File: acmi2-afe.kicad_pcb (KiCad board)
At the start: 10 copper layers, 241.3 x 101.6 mm, 117 parts, among them J1 6469028-1, J2 6469028-1, J3 6469028-1, J4 Conn_Coaxial, J5 5499922-4, J6 39301022, J7 5499922-4, Q1 NX7002BKW, T1 T1-1T-KK81, U1 200MHz, U2 LTC2107CUK-PBF, U3 TPS7A8500RGRT, U4 TPSM82866AA0HRDMR, U5 TPS7A8500RGRT, U6 TPS259540DSGR, U7 SN74LVC16T245DGGR, U8 CAT25320VI-GT3

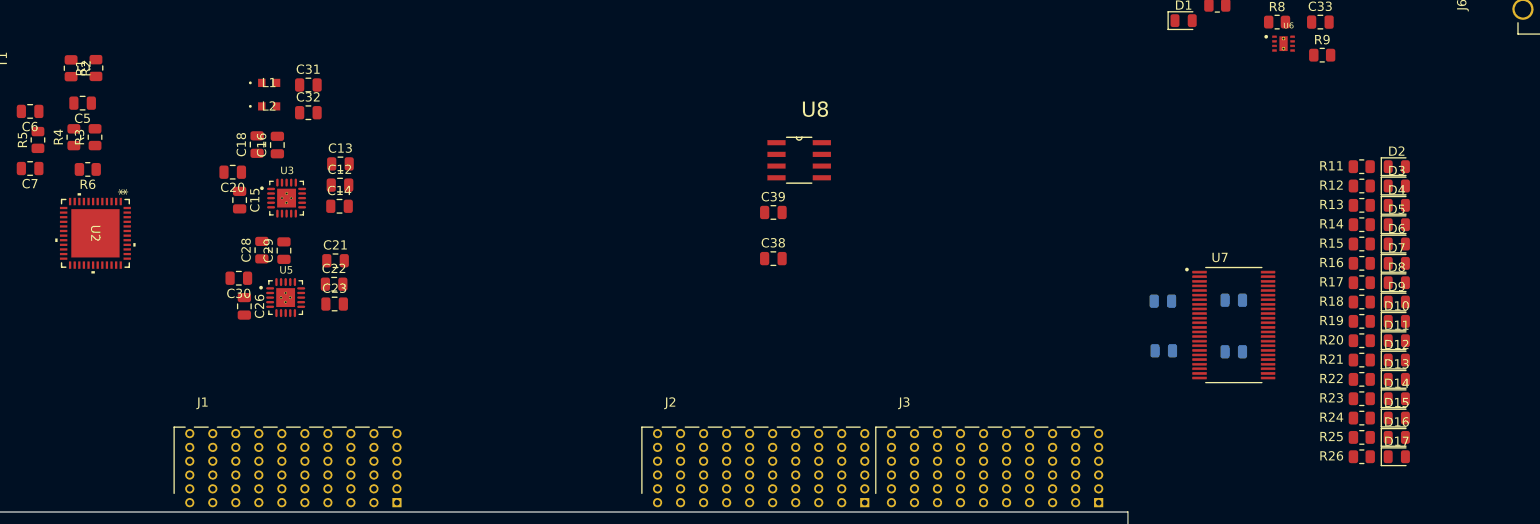
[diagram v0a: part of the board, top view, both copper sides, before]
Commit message: Untangled adc data connections
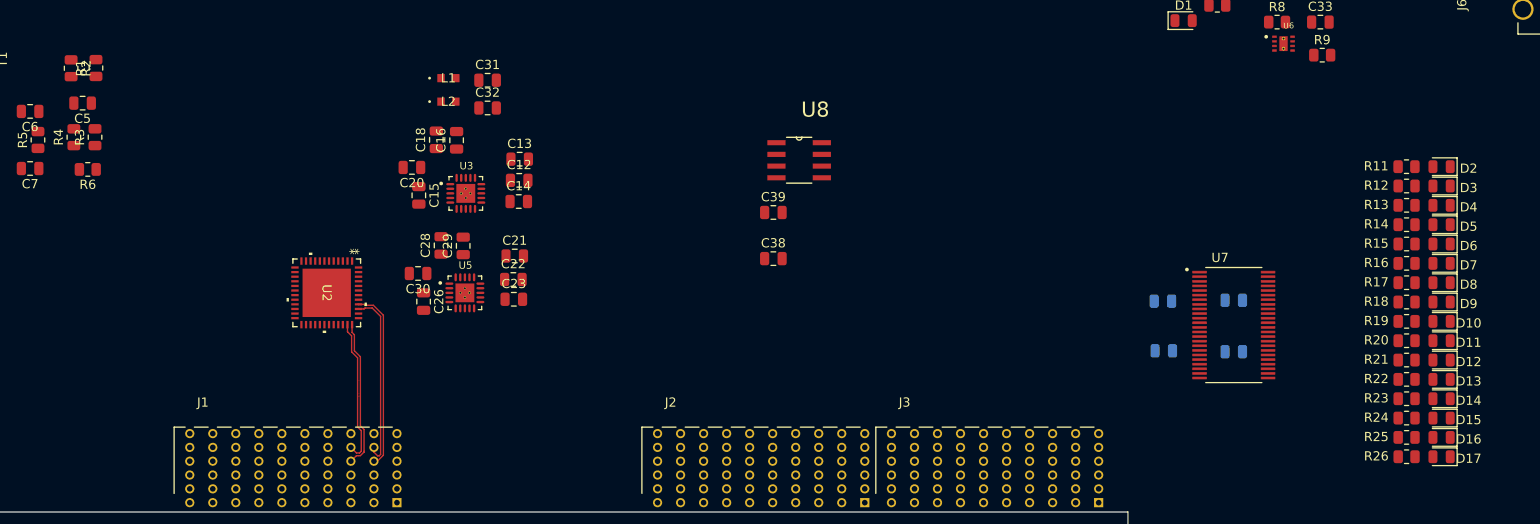
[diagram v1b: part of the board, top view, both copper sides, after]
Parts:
- moved U2 25.9 mm to (159.2, 298.5)
- moved C12 19.5 mm to (180.1, 286.3)
- moved C13 19.5 mm to (180.2, 284.0)
- moved C14 19.5 mm to (180.1, 288.6)
- moved C16 19.5 mm to (173.3, 281.9)
- moved C18 19.5 mm to (171.1, 281.9)
- moved C21 19.5 mm to (179.6, 294.5)
- moved C22 19.5 mm to (179.5, 297.1)
- moved C26 19.5 mm to (169.7, 299.4)
- moved C28 19.5 mm to (171.6, 293.4)
- moved C30 19.5 mm to (169.1, 296.4)
- moved C31 19.5 mm to (176.7, 275.4)
- moved C32 19.5 mm to (176.7, 278.4)
- moved L1 19.5 mm to (172.4, 275.2)
- moved L2 19.5 mm to (172.4, 277.7)
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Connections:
- J1 pad A1: /adc/D0_P -> /adc/CSN
- J1 pad A2: /adc/D4_P -> /adc/SDI
- J1 pad A3: /adc/D8_P -> /adc/D14_P
- J1 pad A4: /adc/D12_P -> /adc/D10_P
- J1 pad A6: /adc/SDO -> /adc/D6_P
- J1 pad A7: unconnected-(J1-PadA7) -> /adc/D2_P
- J1 pad A8: unconnected-(J1-PadA8) -> /adc/SDO
- J1 pad B1: /adc/D0_N -> unconnected-(J1-PadB1)
- J1 pad B2: /adc/D4_N -> unconnected-(J1-PadB2)
- J1 pad B3: /adc/D8_N -> /adc/D14_N
- J1 pad B4: /adc/D12_N -> /adc/D10_N
- J1 pad B6: /adc/SDI -> /adc/D6_N
- J1 pad B7: unconnected-(J1-PadB7) -> /adc/D2_N
- J1 pad C1: /adc/D2_P -> /adc/SCK
- J1 pad C2: /adc/D6_P -> /adc/OF_P
- J1 pad C3: /adc/D10_P -> /adc/D12_P
- J1 pad C4: /adc/D14_P -> unconnected-(J1-PadC4)
- J1 pad C5: /adc/OF_P -> /adc/D8_P
- J1 pad C6: /adc/SCK -> /adc/D4_P
- J1 pad C7: unconnected-(J1-PadC7) -> /adc/D0_P
- J1 pad D1: /adc/D2_N -> unconnected-(J1-PadD1)
- J1 pad D2: /adc/D6_N -> /adc/OF_N
- J1 pad D3: /adc/D10_N -> /adc/D12_N
- J1 pad D4: /adc/D14_N -> unconnected-(J1-PadD4)
- J1 pad D5: /adc/OF_N -> /adc/D8_N
- J1 pad D6: /adc/CSN -> /adc/D4_N
- J1 pad D7: unconnected-(J1-PadD7) -> /adc/D0_N
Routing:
- net /adc/OF_P: track 0.00 -> 19.7 mm
- net /adc/OF_N: track 0.00 -> 19.3 mm
- net /adc/D12_P: track 0.00 -> 16.3 mm
- net /adc/D12_N: track 0.00 -> 15.8 mm

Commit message: push from windows
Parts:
- moved J7 1.40 mm to (111.2, 241.9)
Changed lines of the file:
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@@
 	(footprint "My Footprints:TE_5499922-4"
 		(layer "F.Cu")
-		(at 112.480468 242.555)
+		(at 111.24 241.9)
 		(property "Reference" "J7"
 			(at -8.745 -7.435 0)

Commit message: Finish routing
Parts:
- removed TP5, TP6: GND, My Footprints:TestPoint_RCS-0C
- added C40: 0.1u, Capacitor_SMD:C_0805_2012Metric, F.Cu at (119.4, 294.0)
- C1, C11, C39: moved to B.Cu
- moved G*** 187.4 mm to (87.2, 277.4)
- moved TP2 85.0 mm to (259.4, 332.0)
- moved C17 74.8 mm to (278.6, 320.9), turned to -90 degrees
- moved C19 74.7 mm to (276.4, 320.9), turned to -90 degrees
- moved C38 71.4 mm to (274.2, 320.9), turned to -90 degrees
- moved C24 67.1 mm to (265.9, 322.1), turned to 90 degrees
- moved U4 65.9 mm to (269.9, 320.7), turned to -90 degrees
- moved C25 63.8 mm to (263.6, 322.1), turned to 90 degrees
- moved R7 63.3 mm to (269.6, 316.0)
- moved C27 60.5 mm to (261.3, 322.1), turned to 90 degrees
- moved R9 60.2 mm to (285.4, 330.1), turned to -90 degrees
- moved R8 58.9 mm to (281.4, 324.8), turned to -90 degrees
- moved C33 58.6 mm to (285.4, 324.8), turned to -90 degrees
- moved Q1 57.7 mm to (276.7, 315.2)
- moved C10 57.1 mm to (166.2, 298.1), turned to 90 degrees
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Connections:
- net Net-(J6-Pad2) renamed /Regulators/+5VIN
- net Net-(U3-EN) renamed /Regulators/+3.3v_U3
- net Net-(U5-EN) renamed /Regulators/+3.3v_U5
- C3 pad 2: /adc/adc_clk_p -> /adc/ADC_CLK_P
- C4 pad 2: /adc/adc_clk_n -> /adc/ADC_CLK_N
- J2 pad A1: /Fault LED's/fault_led0 -> unconnected-(J2-PadA1)
- J2 pad A2: /Fault LED's/fault_led4 -> unconnected-(J2-PadA2)
- J2 pad A3: /Fault LED's/fault_led8 -> unconnected-(J2-PadA3)
- J2 pad A4: /Fault LED's/fault_led12 -> unconnected-(J2-PadA4)
- J2 pad B1: /Fault LED's/fault_led1 -> unconnected-(J2-PadB1)
- J2 pad B2: /Fault LED's/fault_led5 -> unconnected-(J2-PadB2)
- J2 pad B3: /Fault LED's/fault_led9 -> unconnected-(J2-PadB3)
- J2 pad B4: /Fault LED's/fault_led13 -> unconnected-(J2-PadB4)
- J2 pad C1: /Fault LED's/fault_led2 -> unconnected-(J2-PadC1)
- J2 pad C10: unconnected-(J2-PadC10) -> /Fault LED's/fault_led1
- J2 pad C2: /Fault LED's/fault_led6 -> unconnected-(J2-PadC2)
- J2 pad C3: /Fault LED's/fault_led10 -> /Fault LED's/fault_led15
- J2 pad C4: /Fault LED's/fault_led14 -> /Fault LED's/fault_led13
- J2 pad C5: unconnected-(J2-PadC5) -> /Fault LED's/fault_led11
- J2 pad C6: unconnected-(J2-PadC6) -> /Fault LED's/fault_led9
- J2 pad C7: unconnected-(J2-PadC7) -> /Fault LED's/fault_led7
- J2 pad C8: unconnected-(J2-PadC8) -> /Fault LED's/fault_led5
- J2 pad C9: unconnected-(J2-PadC9) -> /Fault LED's/fault_led3
- J2 pad D1: /Fault LED's/fault_led3 -> unconnected-(J2-PadD1)
- J2 pad D10: unconnected-(J2-PadD10) -> /Fault LED's/fault_led0
- J2 pad D2: /Fault LED's/fault_led7 -> unconnected-(J2-PadD2)
- J2 pad D3: /Fault LED's/fault_led11 -> /Fault LED's/fault_led14
- J2 pad D4: /Fault LED's/fault_led15 -> /Fault LED's/fault_led12
- J2 pad D5: unconnected-(J2-PadD5) -> /Fault LED's/fault_led10
- J2 pad D6: unconnected-(J2-PadD6) -> /Fault LED's/fault_led8
- J2 pad D7: unconnected-(J2-PadD7) -> /Fault LED's/fault_led6
- J2 pad D8: unconnected-(J2-PadD8) -> /Fault LED's/fault_led4
- J2 pad D9: unconnected-(J2-PadD9) -> /Fault LED's/fault_led2
- J3 pad A1: /Pulser Interface/tp_pos0 -> /Pulser Interface/tp_neg4
- J3 pad A10: /Relay Board Interface/spare4 -> /Relay Board Interface/faultn
- J3 pad A2: /Pulser Interface/tp_pos4 -> /Pulser Interface/tp_neg0
- J3 pad A3: /Pulser Interface/tp_neg3 -> /Pulser Interface/tp_pos1
- J3 pad A8: /Relay Board Interface/fault_rdbk -> /Relay Board Interface/spare3
- J3 pad A9: /Relay Board Interface/spare0 -> /Relay Board Interface/keylock
- J3 pad B1: /Pulser Interface/tp_pos1 -> /Pulser Interface/tp_neg3
- J3 pad B2: /Pulser Interface/tp_neg0 -> /Pulser Interface/tp_pos4
- J3 pad B3: /Pulser Interface/tp_neg4 -> /Pulser Interface/tp_pos0
- J3 pad B8: /zuDFE Connectors/fault_reset -> /Relay Board Interface/spare2
- J3 pad B9: /Relay Board Interface/spare1 -> /Relay Board Interface/force_trip
- J3 pad C1: /Pulser Interface/tp_pos2 -> /Pulser Interface/tp_neg2
- J3 pad C2: /Pulser Interface/tp_neg1 -> /Pulser Interface/tp_pos3
- J3 pad C8: /Relay Board Interface/force_trip -> /Relay Board Interface/spare1
- J3 pad C9: /Relay Board Interface/spare2 -> /Relay Board Interface/fault_reset
- J3 pad D1: /Pulser Interface/tp_pos3 -> /Pulser Interface/tp_neg1
- J3 pad D2: /Pulser Interface/tp_neg2 -> /Pulser Interface/tp_pos2
- J3 pad D7: /Relay Board Interface/faultn -> /Relay Board Interface/spare4
- J3 pad D8: /Relay Board Interface/keylock -> /Relay Board Interface/spare0
- J3 pad D9: /Relay Board Interface/spare3 -> /Relay Board Interface/fault_rdbk
- R3 pad 1: Net-(U2-AIN+) -> /adc/AIN_N
- R4 pad 1: Net-(U2-AIN-) -> /adc/AIN_P
- R6 pad 1: Net-(U2-AIN+) -> /adc/AIN_N
- R6 pad 2: Net-(U2-AIN-) -> /adc/AIN_P
- T1 pad 4: Net-(C2-Pad2) -> Net-(C40-Pad2)
- T1 pad 6: GND -> Net-(C2-Pad2)
- U2 pad 14: /adc/adc_clk_p -> /adc/ADC_CLK_N
- U2 pad 15: /adc/adc_clk_n -> /adc/ADC_CLK_P
- U2 pad 8: Net-(U2-AIN+) -> /adc/AIN_P
- U2 pad 9: Net-(U2-AIN-) -> /adc/AIN_N
- U3 pad V1: (no net) -> GND
- U3 pad V2: (no net) -> GND
- U3 pad V3: (no net) -> GND
- U3 pad V4: (no net) -> GND
- U4 pad 24: (no net) -> GND
- U4 pad 25: (no net) -> GND
- U4 pad 26: (no net) -> GND
- U4 pad 27: (no net) -> GND
- U5 pad V1: (no net) -> GND
- U5 pad V2: (no net) -> GND
- U5 pad V3: (no net) -> GND
- U5 pad V4: (no net) -> GND
- U6 pad 10: (no net) -> GND
- U6 pad 11: (no net) -> GND
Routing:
- net GND: track 17.4 -> 195.0 mm, vias 6 -> 92
- net /Relay Board Interface/faultn: track 0.00 -> 145.6 mm
- net /Relay Board Interface/keylock: track 0.00 -> 141.5 mm
- net /Relay Board Interface/force_trip: track 0.00 -> 140.9 mm
- net /Relay Board Interface/fault_reset: track 0.00 -> 139.2 mm
- net /Relay Board Interface/fault_rdbk: track 0.00 -> 138.4 mm
- net /Relay Board Interface/spare2: track 0.00 -> 135.0 mm
- net /Relay Board Interface/spare0: track 0.00 -> 133.9 mm
- net /Relay Board Interface/spare3: track 0.00 -> 133.5 mm
- net /Relay Board Interface/spare1: track 0.00 -> 133.5 mm
- net /Relay Board Interface/spare4: track 0.00 -> 126.9 mm
- net /Regulators/afe_pwrenb: track 0.00 -> 117.9 mm, vias 0 -> 1
- net /Fault LED's/fault_led0: track 0.00 -> 85.2 mm, vias 0 -> 1
- net /Fault LED's/fault_led1: track 0.00 -> 84.3 mm, vias 0 -> 1
- net /Fault LED's/fault_led2: track 0.00 -> 81.3 mm, vias 0 -> 1
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- added copper zone on F.Cu, net +1.8V
- added copper zone on In2.Cu, net +1.8V
- added copper zone on F.Cu, net +2.5V
- added copper zone on F.Cu, net +3.3V
- added copper zone on In2.Cu, net +3.3V
- added copper zone on F.Cu, net +5.0V
- added copper zone on F.Cu, net /Regulators/+3.3v_U3
- added copper zone on F.Cu, net /Regulators/+3.3v_U5
- added copper zone on F.Cu, net /Regulators/+5VIN
- added copper zone on F.Cu, net GND
- added copper zone on In2.Cu, net GND
- added copper zone on In4.Cu, net GND
- removed copper zone on In3.Cu, net GND
- removed copper zone on In6.Cu, net GND
- removed copper zone on In8.Cu, net GND
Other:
- board size 241.3 x 101.6 mm -> 241.3 x 76.2 mm
- copper layers 10 -> 6

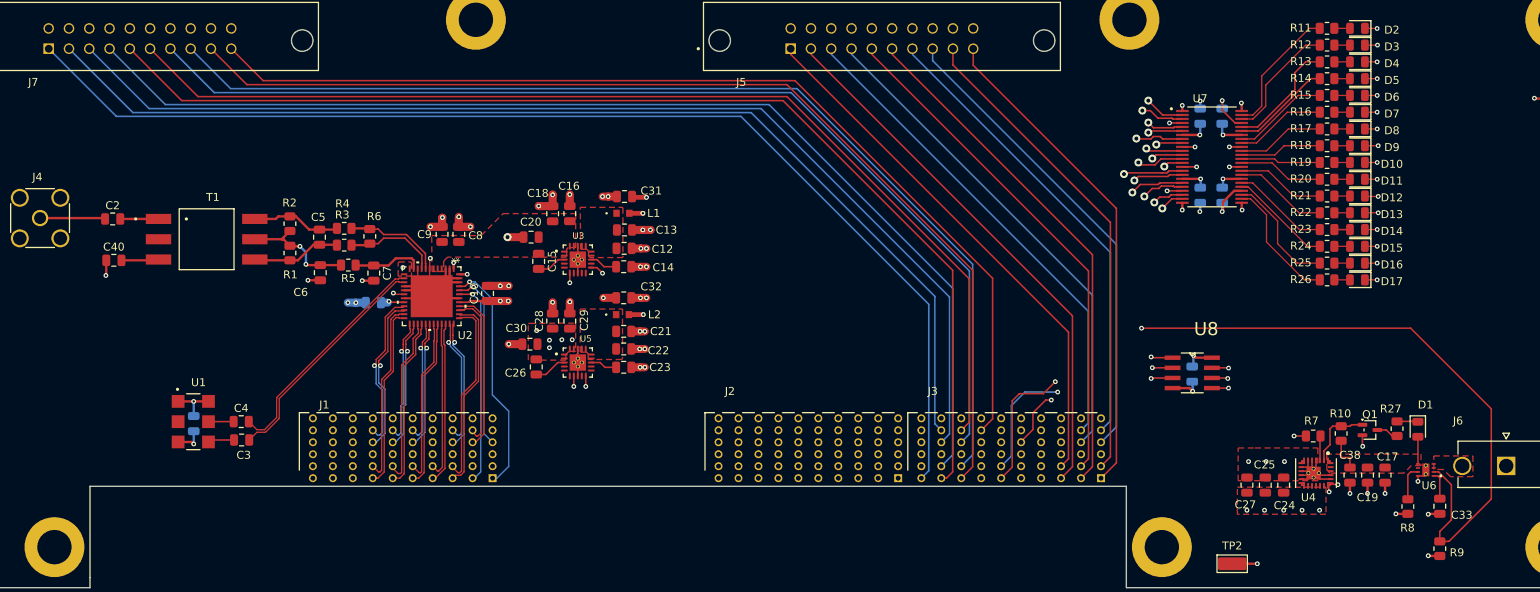
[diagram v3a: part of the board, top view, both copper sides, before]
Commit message: Add watchdog window IC
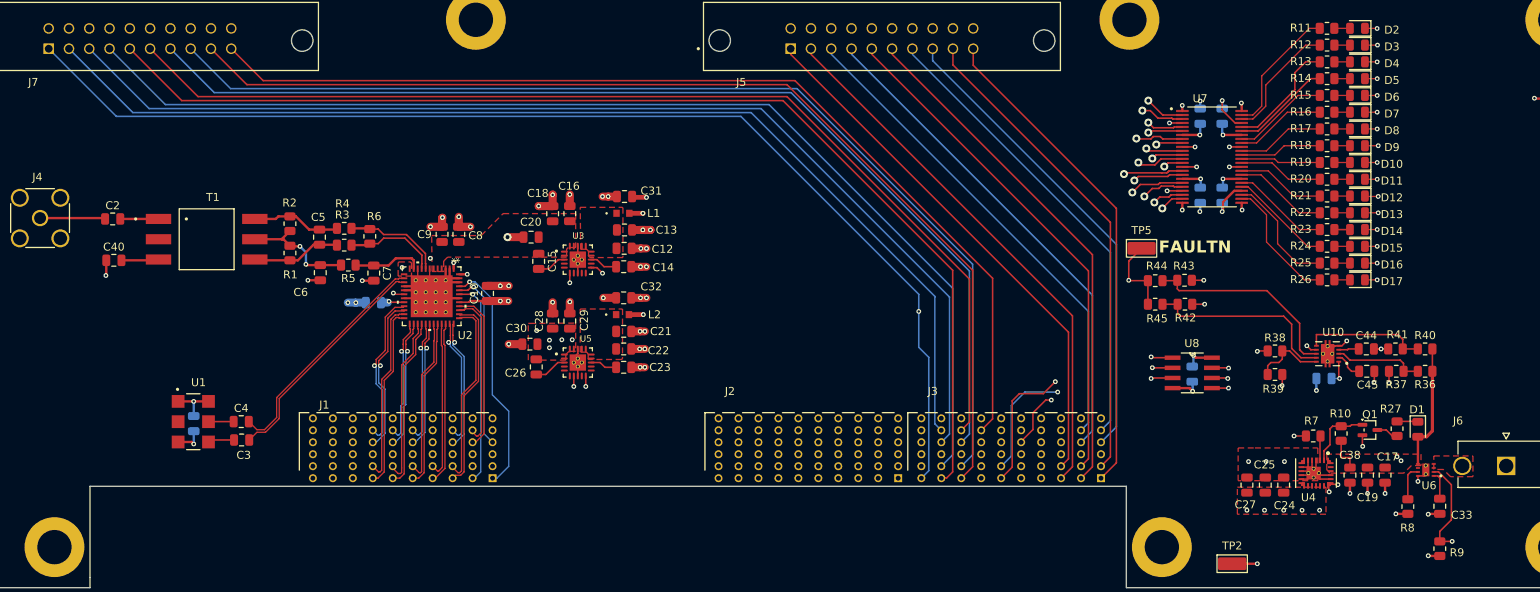
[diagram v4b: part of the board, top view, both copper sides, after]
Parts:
- added C44: 0.1u, Capacitor_SMD:C_0805_2012Metric, F.Cu at (276.2, 305.1)
- added C45: 22nF, Capacitor_SMD:C_0805_2012Metric, F.Cu at (276.3, 307.9)
- added C46: 0.1u, Capacitor_SMD:C_0805_2012Metric, B.Cu at (270.9, 308.8)
- added R36: 10K, Resistor_SMD:R_0805_2012Metric, F.Cu at (283.6, 307.9)
- added R37: 10K, Resistor_SMD:R_0805_2012Metric, F.Cu at (280.0, 307.9)
- added R38: 10K, Resistor_SMD:R_0805_2012Metric, F.Cu at (264.8, 305.4)
- added R39: 10K, Resistor_SMD:R_0805_2012Metric, F.Cu at (264.8, 308.3)
- added R40: 10K, Resistor_SMD:R_0805_2012Metric, F.Cu at (283.6, 305.1)
- added R41: 10K, Resistor_SMD:R_0805_2012Metric, F.Cu at (279.9, 305.1)
- added R42: 1K, Resistor_SMD:R_0805_2012Metric, F.Cu at (253.5, 299.5)
- added R43: 1K, Resistor_SMD:R_0805_2012Metric, F.Cu at (253.5, 296.5)
- added R44: 0, Resistor_SMD:R_0805_2012Metric, F.Cu at (249.8, 296.6)
- added R45: 0, Resistor_SMD:R_0805_2012Metric, F.Cu at (249.8, 299.5)
- added TP5: faultn, My Footprints:TestPoint_RCS-0C, F.Cu at (248.1, 292.5)
- added U10: TPS3850H50DRCR, My Footprints:TPS3850_DRCR, F.Cu at (271.4, 305.7)
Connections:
- J3 pad A7: unconnected-(J3-PadA7) -> /Relay Board Interface/wdi
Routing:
- net /Relay Board Interface/wdi: track 0.00 -> 55.5 mm, vias 0 -> 1
- net /Relay Board Interface/faultn: track 145.6 -> 183.6 mm, vias 0 -> 2
- net +5.0V: track 7.86 -> 36.9 mm, vias 0 -> 3
- net Net-(U10-WDO): track 0.00 -> 25.7 mm
- net Net-(U10-RESET): track 0.00 -> 24.6 mm
- net Net-(U10-SET1): track 0.00 -> 15.5 mm
- net Net-(U10-SET0): track 0.00 -> 11.4 mm
- net GND: track 195.0 -> 204.5 mm, vias 92 -> 98
- net Net-(U10-SENSE): track 0.00 -> 9.13 mm
- net +3.3V: track 23.6 -> 28.0 mm, vias 13 -> 16
- net Net-(U10-CWD): track 0.00 -> 3.55 mm
- net /Regulators/afe_pwrenb: track 117.9 -> 120.5 mm
- net Net-(U10-CRST): track 0.00 -> 2.54 mm
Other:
- board text added: "FAULTN"

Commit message: Finish BOM
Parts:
- C1: value 10p -> 0.1u
- J4: value Conn_Coaxial -> 132134
